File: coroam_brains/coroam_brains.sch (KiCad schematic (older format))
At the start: 56 parts, among them J1 OpenCirc, J2 12V_in, J3 RF_pwr, U1 L7805, U2 mini_esp32

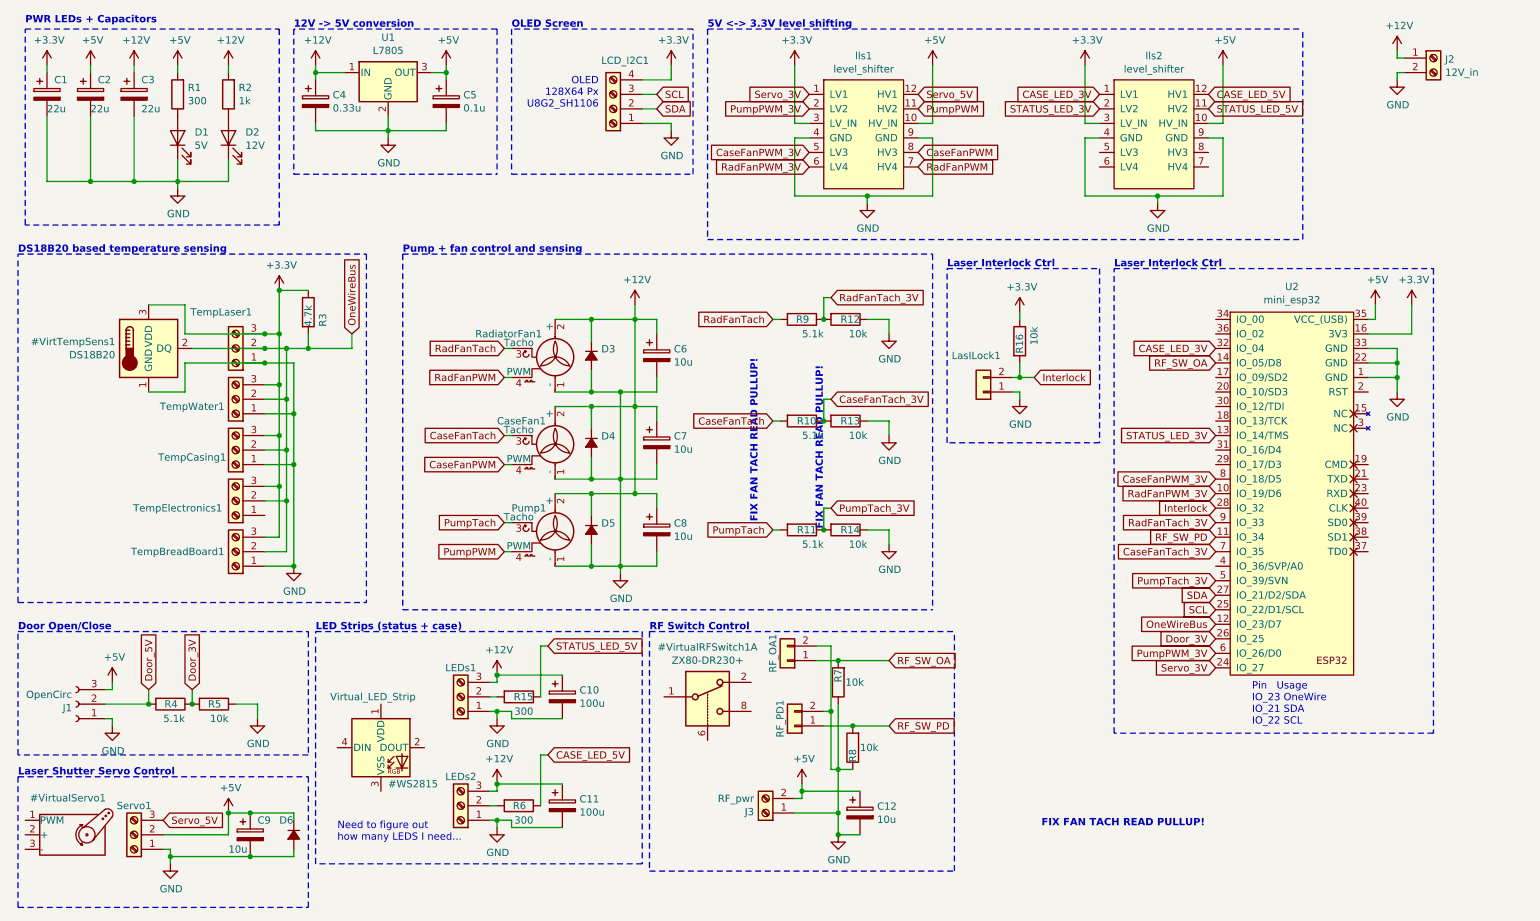
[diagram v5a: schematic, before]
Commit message: brains schematic debugged, now for the design
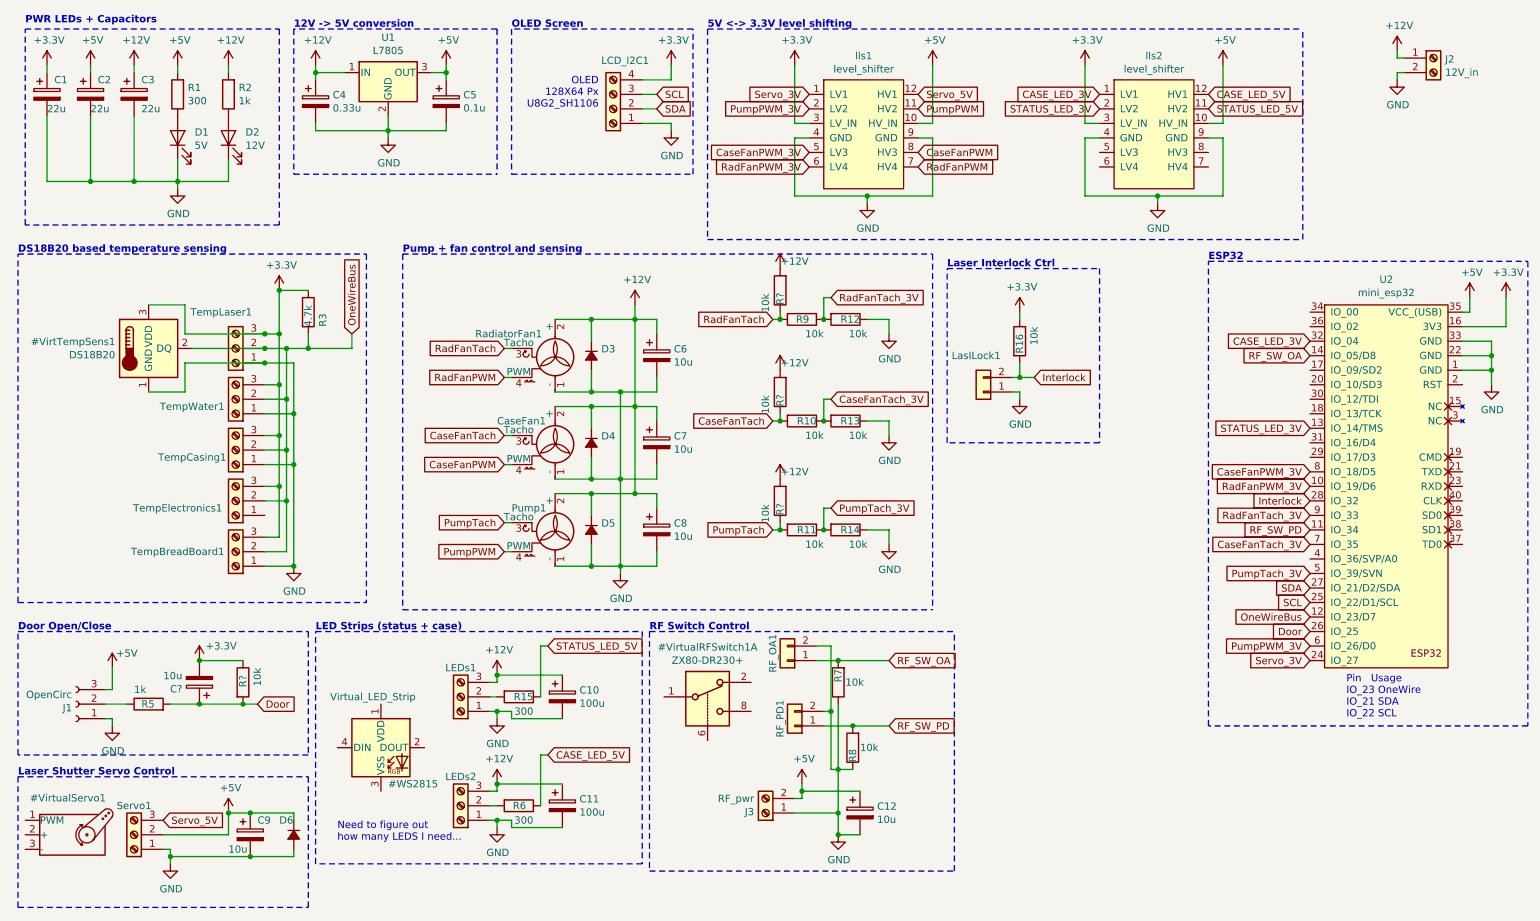
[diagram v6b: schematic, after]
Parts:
- removed R4: 5.1k, Resistor_SMD:R_2010_5025Metric_Pad1.52x2.65mm_HandSolder, symbol coroam_brains-rescue:R-Device
- added C?: 10u, Capacitor_THT:CP_Radial_D5.0mm_P2.50mm, symbol coroam_brains-rescue:CP-Device
- added R? (x4): 10k, Resistor_SMD:R_2010_5025Metric_Pad1.52x2.65mm_HandSolder, symbol coroam_brains-rescue:R-Device
- R10, R11, R9: value 5.1k -> 10k
- R5: value 10k -> 1k; footprint Resistor_SMD:R_2010_5025Metric_Pad1.52x2.65mm_HandSolder -> Resistor_THT:R_Axial_DIN0207_L6.3mm_D2.5mm_P2.54mm_Vertical
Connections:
- net +12V: now also R?.2, R?.2, R?.2
- net +3V3: now also C?.2, R?.1
- net CaseFanTach: now also R?.1
- net GND: no longer R5.1
- net PumpTach: now also R?.1
- net RadFanTach: now also R?.1
- net Door_3V renamed Door
- net Door: now also C?.1, R?.2
- net Door_5V: no longer names the net of J1.2 (Pin_2)
- net Door_5V: now also R5.1
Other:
- note added: "ESP32\n"
- note removed: "FIX FAN TACH READ PULLUP!\n"
- moved on the sheet: R5, U2
